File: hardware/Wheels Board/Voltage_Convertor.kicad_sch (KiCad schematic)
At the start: 28 parts, among them U4 TPS5405DR

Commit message: Rev a final draft
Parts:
- removed TP1: 24V_EXT, TestPoint:TestPoint_Pad_1.0x1.0mm, symbol Connector:TestPoint
- removed TP4: 5V_USB, TestPoint:TestPoint_Pad_1.0x1.0mm, symbol Connector:TestPoint
- renumbered TP1 to TP14
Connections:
- net FAULT is gone; now on net GND: D9.1 (K)
- net STAT is gone; now on net GND: D11.1 (K)

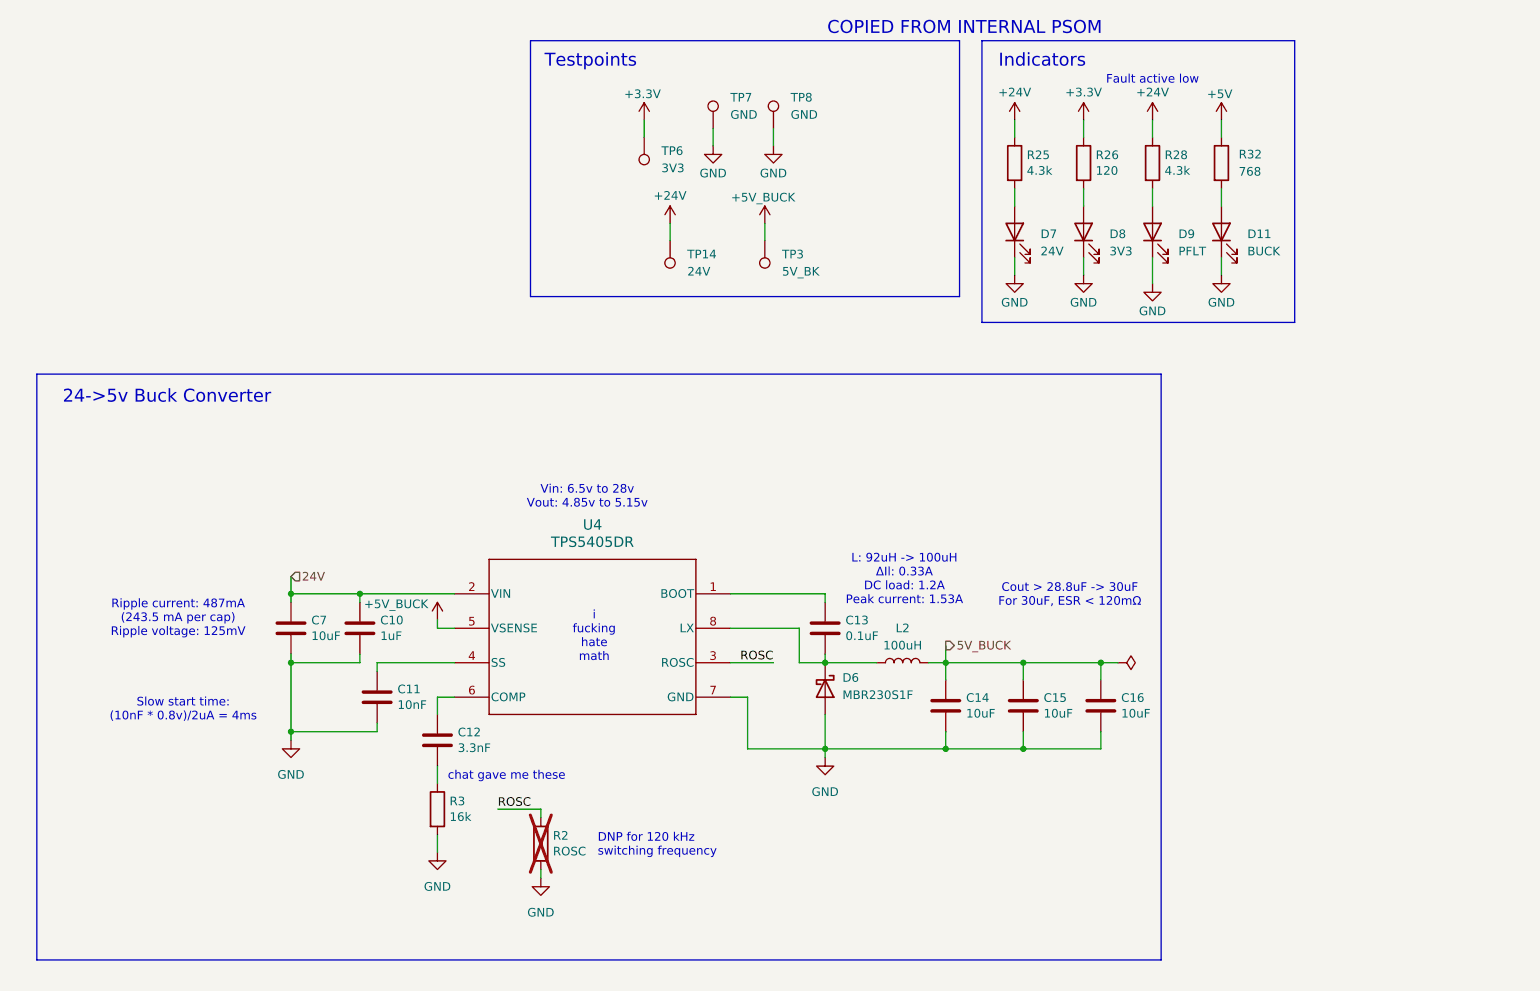
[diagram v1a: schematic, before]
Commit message: +op amp, breakout, footprints
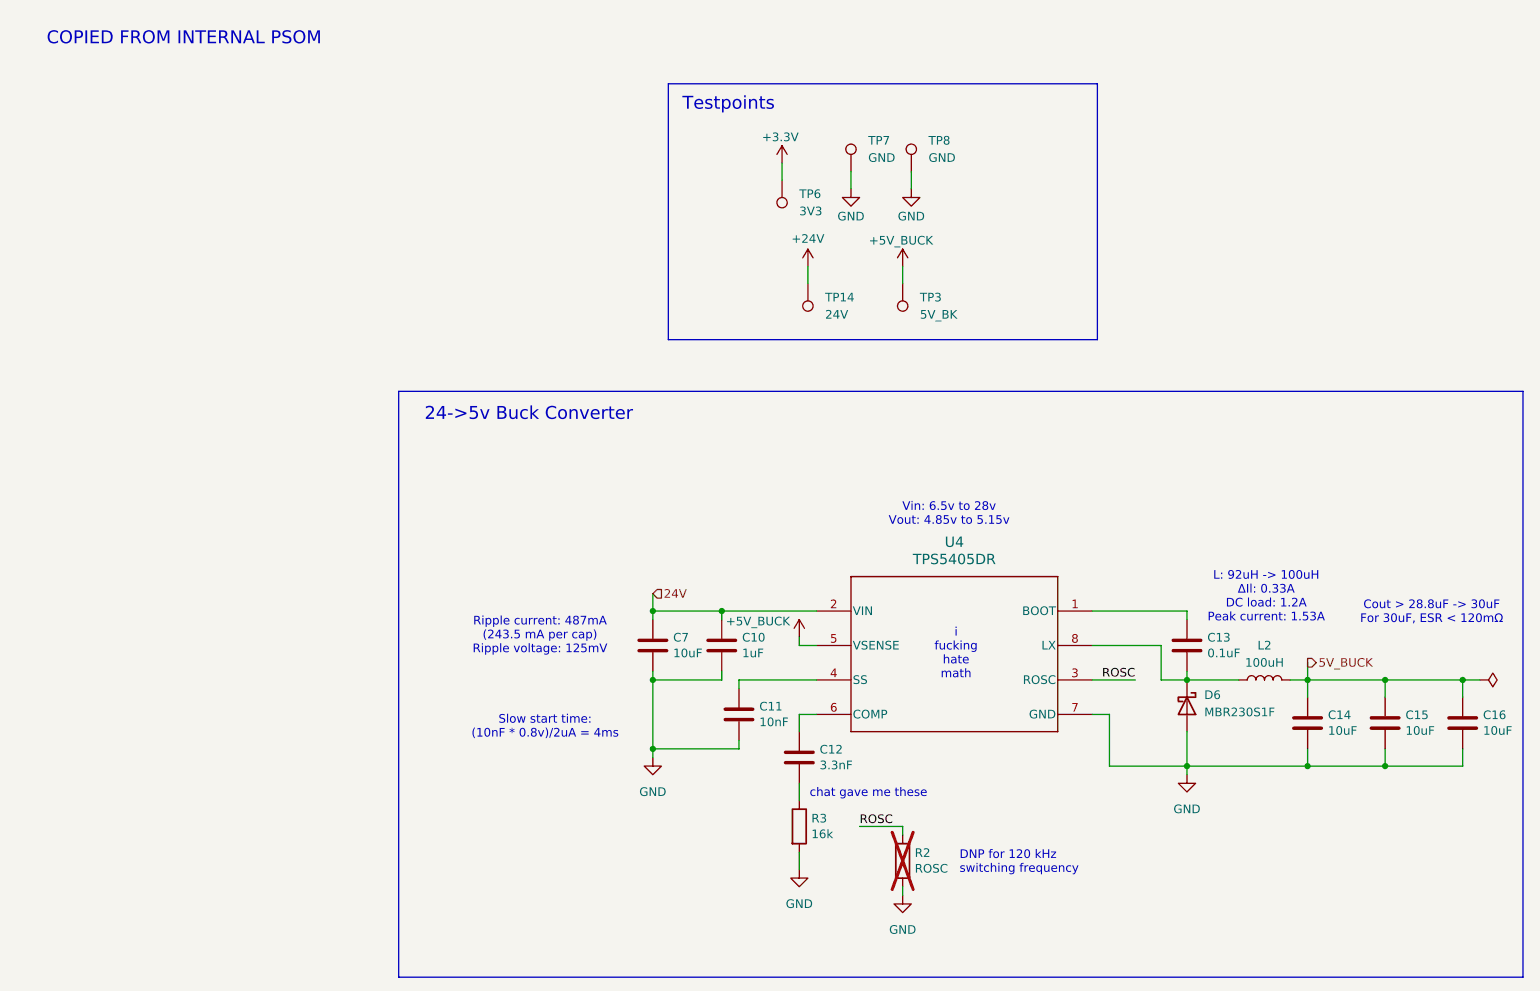
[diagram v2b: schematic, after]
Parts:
- removed D11: BUCK, LED_SMD:LED_0603_1608Metric_Pad1.05x0.95mm_HandSolder, symbol Device:LED
- removed D7: 24V, LED_SMD:LED_0603_1608Metric_Pad1.05x0.95mm_HandSolder, symbol Device:LED
- removed D8: 3V3, LED_SMD:LED_0603_1608Metric_Pad1.05x0.95mm_HandSolder, symbol Device:LED
- removed D9: PFLT, LED_SMD:LED_0603_1608Metric_Pad1.05x0.95mm_HandSolder, symbol Device:LED
- removed R25, R28: 4.3k, Resistor_SMD:R_0603_1608Metric_Pad0.98x0.95mm_HandSolder, symbol Device:R
- removed R26: 120, Resistor_SMD:R_0603_1608Metric_Pad0.98x0.95mm_HandSolder, symbol Device:R
- removed R32: 768, Resistor_SMD:R_0603_1608Metric_Pad0.98x0.95mm_HandSolder, symbol Device:R
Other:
- note removed: "Fault active low"
- note removed: "Indicators"
- moved on the sheet: C10, C11, C12, C13, C14, C15, C16, C7, D6, L2, R2, R3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

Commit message: switched to pads for hall sensor wires
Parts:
- C14, C15, C16, C7: footprint Capacitor_SMD:C_0805_2012Metric_Pad1.18x1.45mm_HandSolder -> Capacitor_SMD:C_0603_1608Metric_Pad1.08x0.95mm_HandSolder
- D6: footprint Diode_SMD:D_SOD-123F -> Diode_SMD:D_SOD-323_HandSoldering
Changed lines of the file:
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@@
 			)
 		)
-		(property "Footprint" "Capacitor_SMD:C_0805_2012Metric_Pad1.18x1.45mm_HandSolder"
+		(property "Footprint" "Capacitor_SMD:C_0603_1608Metric_Pad1.08x0.95mm_HandSolder"
 			(at 225.7552 120.65 0)
 			(effects
@@
 			)
 		)
-		(property "Footprint" "Capacitor_SMD:C_0805_2012Metric_Pad1.18x1.45mm_HandSolder"
+		(property "Footprint" "Capacitor_SMD:C_0603_1608Metric_Pad1.08x0.95mm_HandSolder"
 			(at 214.3252 120.65 0)
 			(effects
@@
 			)
 		)
-		(property "Footprint" "Capacitor_SMD:C_0805_2012Metric_Pad1.18x1.45mm_HandSolder"
+		(property "Footprint" "Capacitor_SMD:C_0603_1608Metric_Pad1.08x0.95mm_HandSolder"
 			(at 106.3752 109.22 0)
 			(effects
@@
 			)
 		)
-		(property "Footprint" "Diode_SMD:D_SOD-123F"
+		(property "Footprint" "Diode_SMD:D_SOD-323_HandSoldering"
 			(at 184.15 114.3 0)
 			(effects
@@
 			)
 		)
-		(property "Footprint" "Capacitor_SMD:C_0805_2012Metric_Pad1.18x1.45mm_HandSolder"
+		(property "Footprint" "Capacitor_SMD:C_0603_1608Metric_Pad1.08x0.95mm_HandSolder"
 			(at 202.8952 120.65 0)
 			(effects

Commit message: layout planning
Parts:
- removed TP14: 24V, TestPoint:TestPoint_Pad_1.0x1.0mm, symbol Connector:TestPoint
- removed TP3: 5V_BK, TestPoint:TestPoint_Pad_1.0x1.0mm, symbol Connector:TestPoint
- removed TP6: 3V3, TestPoint:TestPoint_Pad_1.0x1.0mm, symbol Connector:TestPoint
- removed TP7, TP8: GND, TestPoint:TestPoint_Pad_1.0x1.0mm, symbol Connector:TestPoint
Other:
- note removed: "Testpoints"

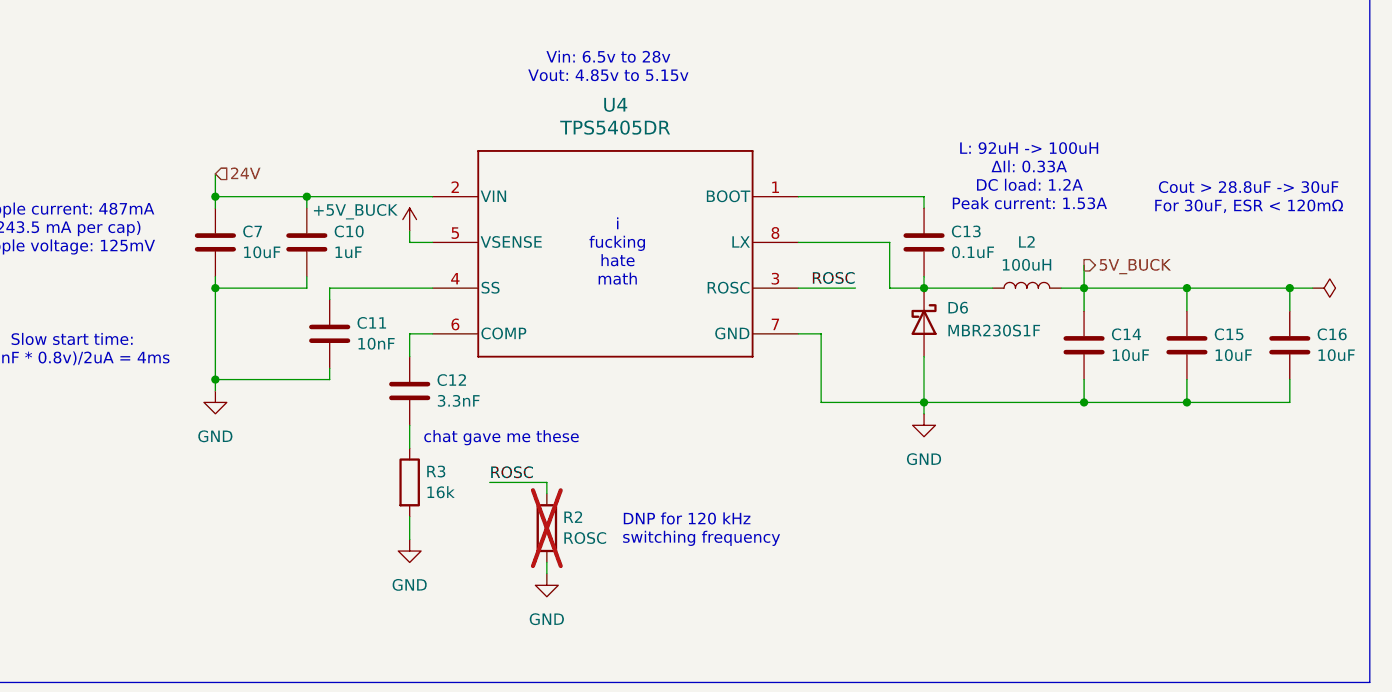
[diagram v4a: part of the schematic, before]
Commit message: review council changes, layout not finalized
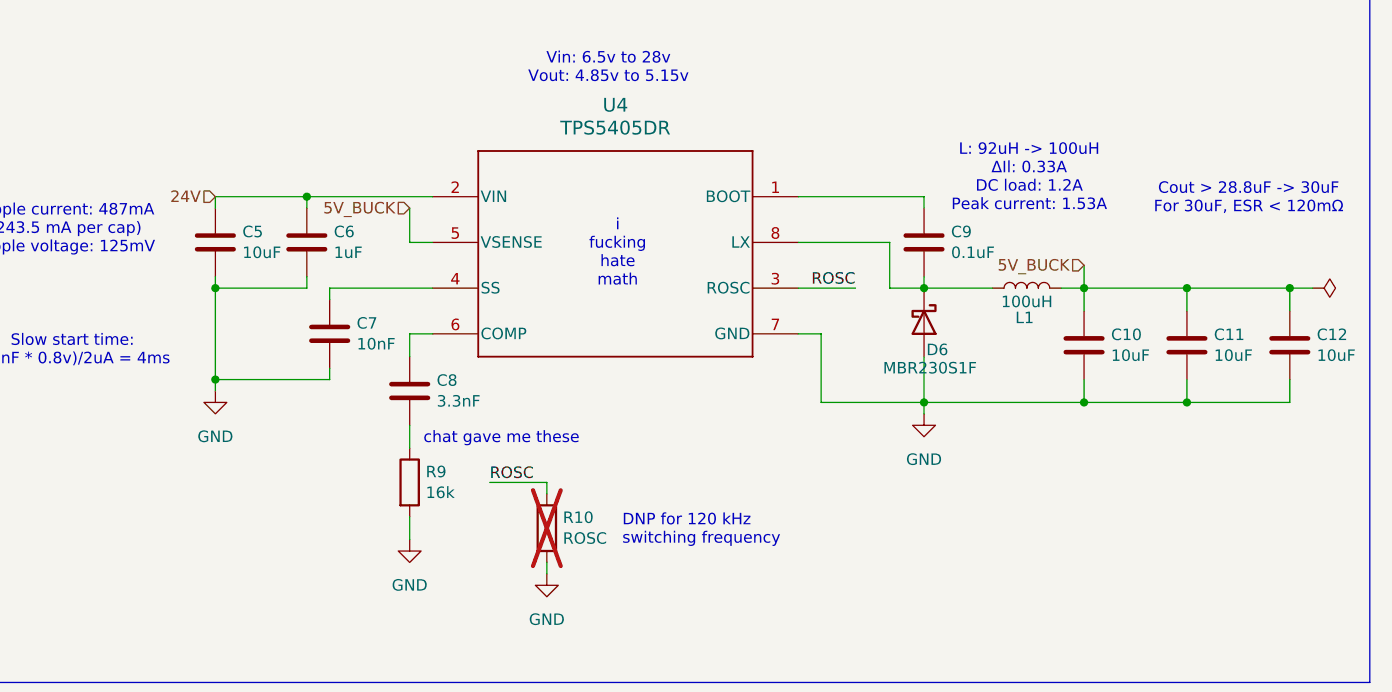
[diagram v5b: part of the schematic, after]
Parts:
- C8: renamed from C12; P/N 06035C332K4T2A -> MSASH168SB5103KTNA01
- D6: P/N SS24FL -> MP01EA06
- renumbered C14 to C10, C15 to C11, C16 to C12, C7 to C5, C10 to C6, C11 to C7, C13 to C9, L2 to L1, R2 to R10, R3 to R9
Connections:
- net +5V_BUCK is gone; now on net 5V_BUCK: U4.5 (VSENSE)

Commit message: final revisions!
i didnt do pn yet
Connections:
- net IND_NODE: now reaches C9.2, D6.1 (K), L1.1, U4.8 (LX)
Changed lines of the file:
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@@
+	(wire
+		(pts
+			(xy 180.34 110.49) (xy 184.15 110.49)
+		)
+		(stroke
+			(width 0)
+			(type default)
+		)
+	)
 	(wire
 		(pts
@@
 		(pts
 			(xy 199.39 110.49) (xy 201.93 110.49)
-		)
-		(stroke
-			(width 0)
-			(type default)
-		)
-	)
-	(wire
-		(pts
-			(xy 180.34 110.49) (xy 184.15 110.49)
 		)
 		(stroke
@@
 		(effects
 			(font
+				(size 1.27 1.27)
+			)
+			(justify left bottom)
+		)
+	)
+	(label "IND_NODE"
+		(at 180.34 110.49 0)
+		(effects
+			(font
